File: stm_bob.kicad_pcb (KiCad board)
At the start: 4 copper layers, 140 x 140 mm, 125 parts, among them J1 Conn_01x02, J10_GPIO1 Conn_01x02, J11_GPIO1 Conn_01x03, J11_SPI1 Conn_01x03, J11_SPI2 Conn_01x03, J2 Conn_01x04_Pin, J3 Conn_01x04_Pin, J4 Conn_01x02_Pin, J5 Conn_01x04_Pin, J6 Conn_01x04_Pin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

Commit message: make mounting holes M3 friendly (3.2mm)
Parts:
- C23: value C -> 10pf
- D1: value D_Zener -> 10V
- H1, H2, H3, H4: footprint MountingHole:MountingHole_2.5mm -> MountingHole:MountingHole_3.2mm_M3
- R10, R12, R14, R17, R2, R4, R6, R8: value 4k7 -> 3k3
- R15, R28: value R -> 1k
- R16: value R -> 47k
- R21: value 1k -> 430
- R25: value R -> 100k
- R26: value R -> 470
- R27: value R -> 430
- R31, R32, R33, R34: value R -> 3k3
- RV1: value R_Potentiometer -> 100k
- moved J1 0.39 mm to (150.3, 35.5)
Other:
- board text added: "."
- board text added: "SW GND +12V"

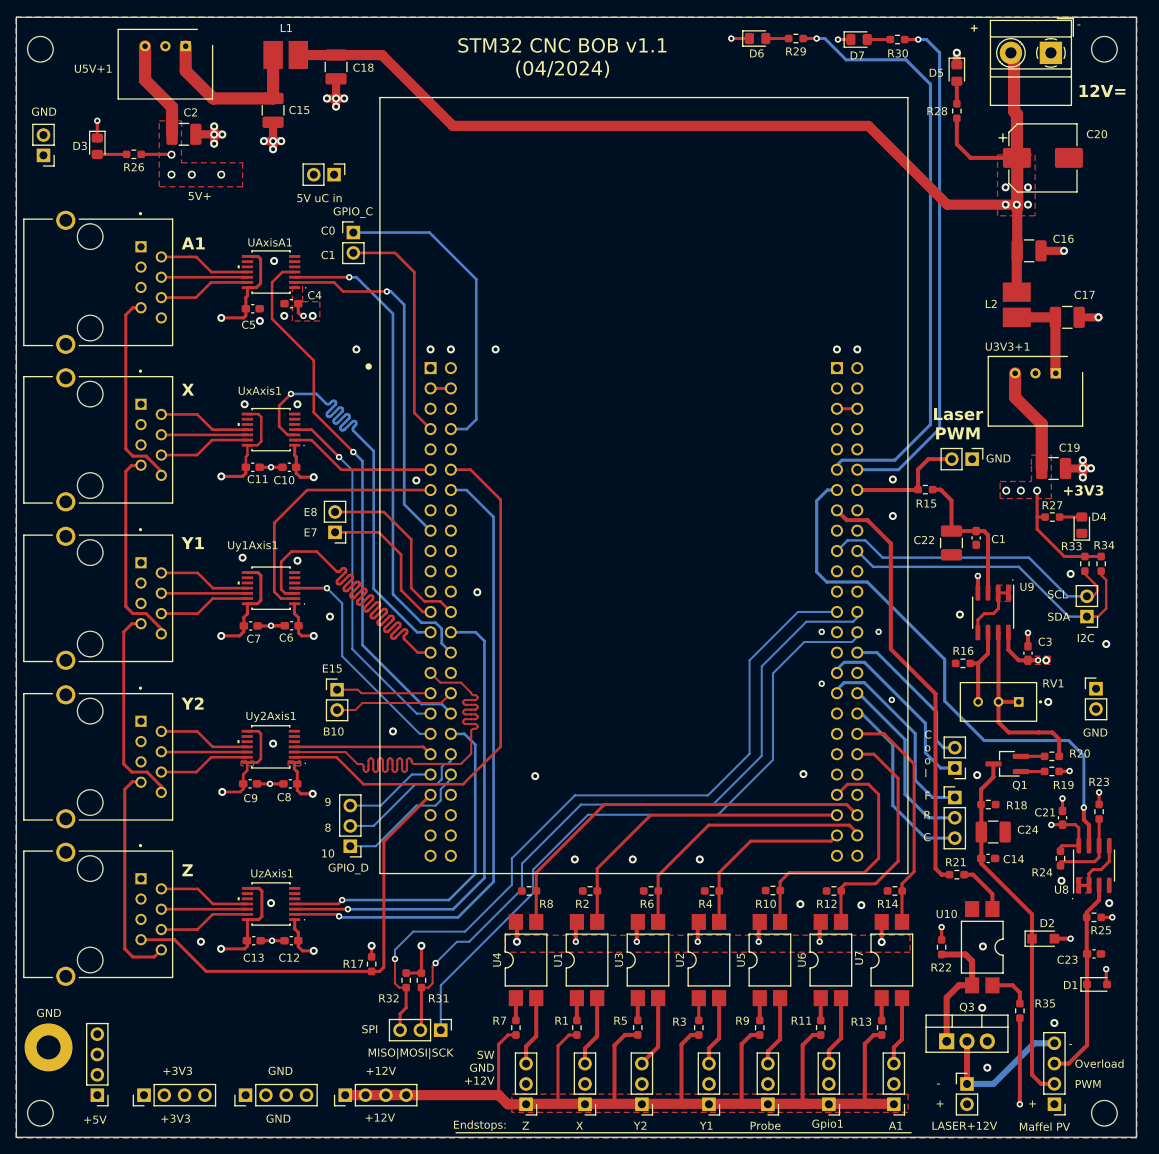
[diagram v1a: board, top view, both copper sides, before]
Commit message: properly connected moved 12V connector
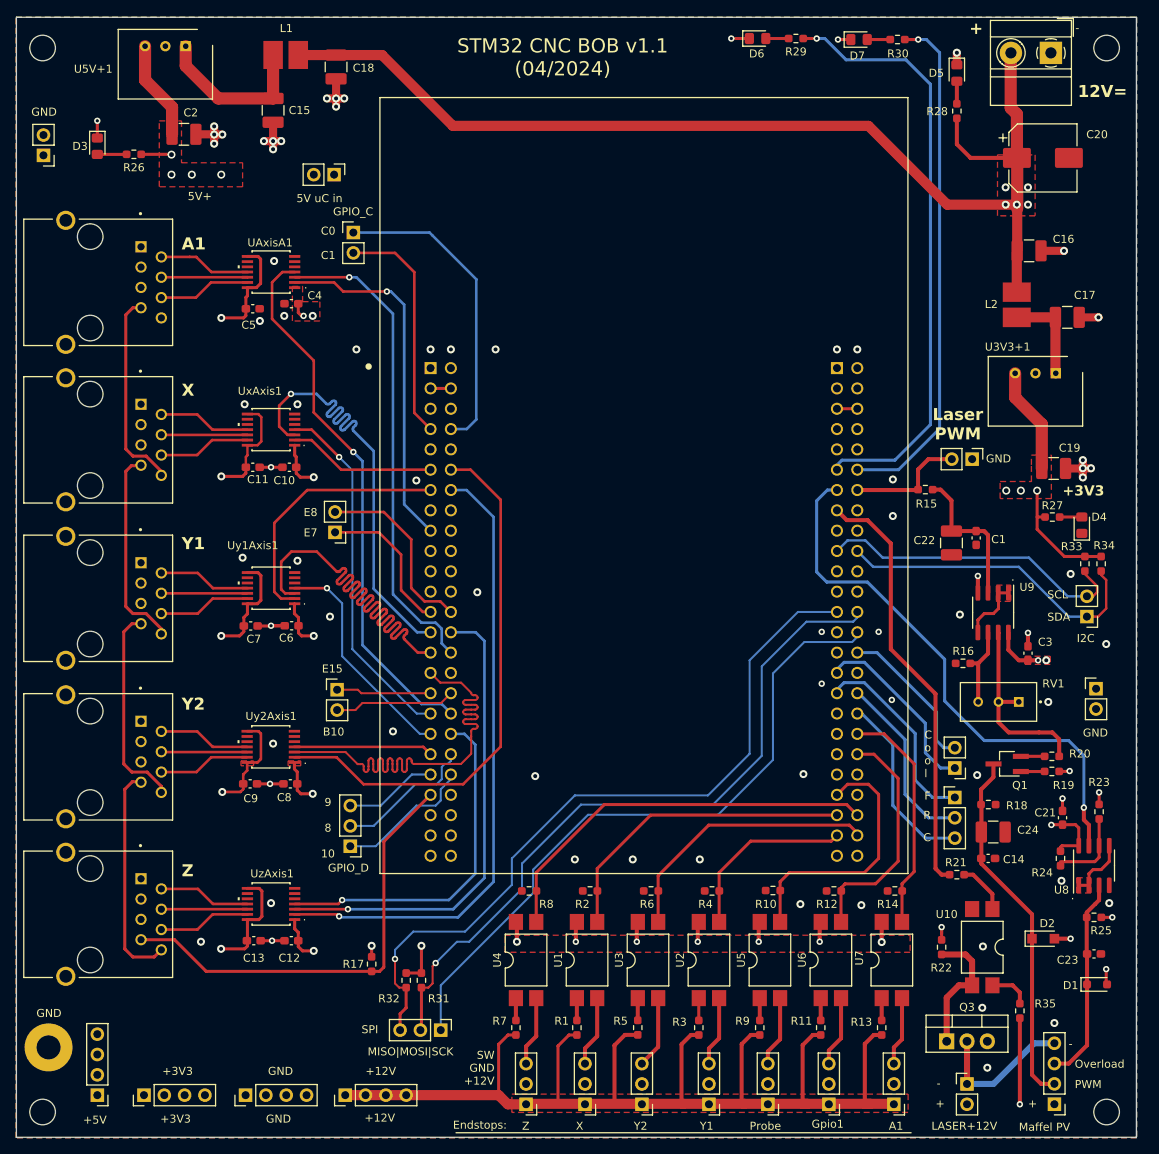
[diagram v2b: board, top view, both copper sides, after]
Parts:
- moved H3 0.32 mm to (157.3, 167.8)
- moved H4 0.32 mm to (157.3, 34.8)
- moved H2 0.32 mm to (24.3, 167.8)
- moved H1 0.32 mm to (24.3, 34.8)
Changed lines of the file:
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@@
   )
   (footprint "MountingHole:MountingHole_3.2mm_M3" (layer "F.Cu")
-    (at 157 168)
+    (at 157.2768 167.8432)
     (descr "Mounting Hole 3.2mm, no annular, M3")
     (tags "mounting hole 3.2mm no annular m3")
@@
   )
   (footprint "MountingHole:MountingHole_3.2mm_M3" (layer "F.Cu")
-    (at 24 168)
+    (at 24.2768 167.8432)
     (descr "Mounting Hole 3.2mm, no annular, M3")
     (tags "mounting hole 3.2mm no annular m3")
@@
   )
   (footprint "MountingHole:MountingHole_3.2mm_M3" (layer "F.Cu")
-    (at 24 35)
+    (at 24.2768 34.8432)
     (descr "Mounting Hole 3.2mm, no annular, M3")
     (tags "mounting hole 3.2mm no annular m3")
@@
   )
   (footprint "MountingHole:MountingHole_3.2mm_M3" (layer "F.Cu")
-    (at 157 35)
+    (at 157.2768 34.8432)
     (descr "Mounting Hole 3.2mm, no annular, M3")
     (tags "mounting hole 3.2mm no annular m3")
@@
     (effects (font (size 1 1) (thickness 0.15)) (justify left bottom))
   )
-  (gr_text "-" (at 153.5684 32.4612) (layer "F.SilkS")
+  (gr_text "-" (at 153.3652 32.9184) (layer "F.SilkS")
     (effects (font (size 1 1) (thickness 0.15)) (justify left bottom))
   )
@@
     (effects (font (size 1 1) (thickness 0.15)) (justify left bottom))
   )
-  (gr_text "+" (at 140.1572 32.9184) (layer "F.SilkS")
-    (effects (font (size 1 1) (thickness 0.25) bold) (justify left bottom))
+  (gr_text "+" (at 140.1064 33.274) (layer "F.SilkS")
+    (effects (font (size 1.5 1.5) (thickness 0.25) bold) (justify left bottom))
   )
   (gr_text "GND\n" (at 23.495 156.083) (layer "F.SilkS")
@@
     (effects (font (size 1 1) (thickness 0.15)) (justify left bottom))
   )
-  (gr_text "MISO|MOSI|SCK" (at 64.897 161.036) (layer "F.SilkS")
+  (gr_text "MISO|MOSI|SCK" (at 64.897 160.8836) (layer "F.SilkS")
     (effects (font (size 1 1) (thickness 0.15)) (justify left bottom))
   )
@@
   (segment (start 111.6584 159.3596) (end 111.6584 166.5122) (width 0.508) (layer "F.Cu") (net 3))
   (segment (start 104.3432 166.817) (end 99.1877 166.817) (width 1.27) (layer "F.Cu") (net 3))
+  (segment (start 145.288 35.4822) (end 145.288 42.338) (width 1.524) (layer "F.Cu") (net 3))
   (segment (start 121.5397 158.214) (end 120.551 158.214) (width 0.508) (layer "F.Cu") (net 3))
   (segment (start 91.0597 158.214) (end 90.071 158.214) (width 0.381) (layer "F.Cu") (net 3))
@@
   (segment (start 152.606911 125.269089) (end 152.654 125.222) (width 0.381) (layer "F.Cu") (net 3))
   (segment (start 122.5557 166.817) (end 119.8372 166.817) (width 0.508) (layer "F.Cu") (net 3))
+  (segment (start 146.0649 43.1149) (end 146.0649 48.578974) (width 1.524) (layer "F.Cu") (net 3))
   (segment (start 127 166.817) (end 130.6837 166.817) (width 1.27) (layer "F.Cu") (net 3))
   (segment (start 146.304 111.379) (end 144.996517 110.071517) (width 0.508) (layer "F.Cu") (net 3))
-  (segment (start 146.0649 48.578974) (end 146.0649 43.1149) (width 1.524) (layer "F.Cu") (net 3))
   (segment (start 146.431 156.1065) (end 146.431 166.878) (width 0.508) (layer "F.Cu") (net 3))
   (segment (start 127.508 44.577) (end 75.565 44.577) (width 1.27) (layer "F.Cu") (net 3))
   (segment (start 98.672548 158.202425) (end 97.067575 158.202425) (width 0.508) (layer "F.Cu") (net 3))
+  (segment (start 145.288 42.338) (end 146.0649 43.1149) (width 1.524) (layer "F.Cu") (net 3))
   (segment (start 111.9632 166.817) (end 107.5697 166.817) (width 1.27) (layer "F.Cu") (net 3))
   (segment (start 69.723 165.735) (end 81.28 165.735) (width 1.27) (layer "F.Cu") (net 3))
-  (segment (start 146.0649 43.1149) (end 145.709 42.759) (width 1.524) (layer "F.Cu") (net 3))
   (segment (start 146.1002 60.195024) (end 146.1002 54.928974) (width 1.27) (layer "F.Cu") (net 3))
   (segment (start 114.9357 166.817) (end 111.9632 166.817) (width 1.27) (layer "F.Cu") (net 3))
@@
   (segment (start 151.3492 125.269089) (end 152.606911 125.269089) (width 0.381) (layer "F.Cu") (net 3))
   (segment (start 129.1597 158.214) (end 128.171 158.214) (width 0.508) (layer "F.Cu") (net 3))
+  (segment (start 145.3172 35.453) (end 145.288 35.4822) (width 1.524) (layer "F.Cu") (net 3))
   (segment (start 104.14 159.385) (end 104.14 166.817) (width 0.508) (layer "F.Cu") (net 3))
   (segment (start 119.2784 159.4866) (end 119.2784 166.817) (width 0.508) (layer "F.Cu") (net 3))
@@
   (segment (start 88.6968 166.6138) (end 88.9 166.817) (width 0.381) (layer "F.Cu") (net 3))
   (segment (start 66.7115 35.7235) (end 60.96 35.7235) (width 1.27) (layer "F.Cu") (net 3))
-  (segment (start 145.709 35.453) (end 145.709 42.759) (width 1.524) (layer "F.Cu") (net 3))
   (segment (start 127.0508 166.7662) (end 127 166.817) (width 0.508) (layer "F.Cu") (net 3))
   (segment (start 105.311 158.214) (end 104.14 159.385) (width 0.508) (layer "F.Cu") (net 3))
@@
   (segment (start 143.002 140.589) (end 140.589 138.176) (width 0.508) (layer "F.Cu") (net 123))
   (segment (start 140.589 138.176) (end 139.4695 138.176) (width 0.508) (layer "F.Cu") (net 123))
-  (segment (start 45.593 41.148) (end 42.164 37.719) (width 1.524) (layer "F.Cu") (net 124))
+  (segment (start 53.086 41.148) (end 46.228 41.148) (width 1.524) (layer "F.Cu") (net 124))
   (segment (start 53.086 35.7124) (end 53.086 41.148) (width 1.524) (layer "F.Cu") (net 124))
-  (segment (start 42.164 37.719) (end 42.164 34.6165) (width 1.524) (layer "F.Cu") (net 124))
-  (segment (start 53.086 41.148) (end 45.593 41.148) (width 1.524) (layer "F.Cu") (net 124))
+  (segment (start 42.164 37.084) (end 42.164 34.6165) (width 1.524) (layer "F.Cu") (net 124))
+  (segment (start 46.228 41.148) (end 42.164 37.084) (width 1.524) (layer "F.Cu") (net 124))
   (segment (start 150.8897 75.467839) (end 150.922398 75.500537) (width 1.27) (layer "F.Cu") (net 125))
   (segment (start 150.876 75.454139) (end 150.922398 75.500537) (width 1.27) (layer "F.Cu") (net 125))
